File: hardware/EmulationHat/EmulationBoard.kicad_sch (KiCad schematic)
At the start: 4 parts, among them J1 Conn_02x16_Top_Bottom, J2 Conn_02x16_Top_Bottom, Q1 FDN340P, U1 ATmega32U4-M

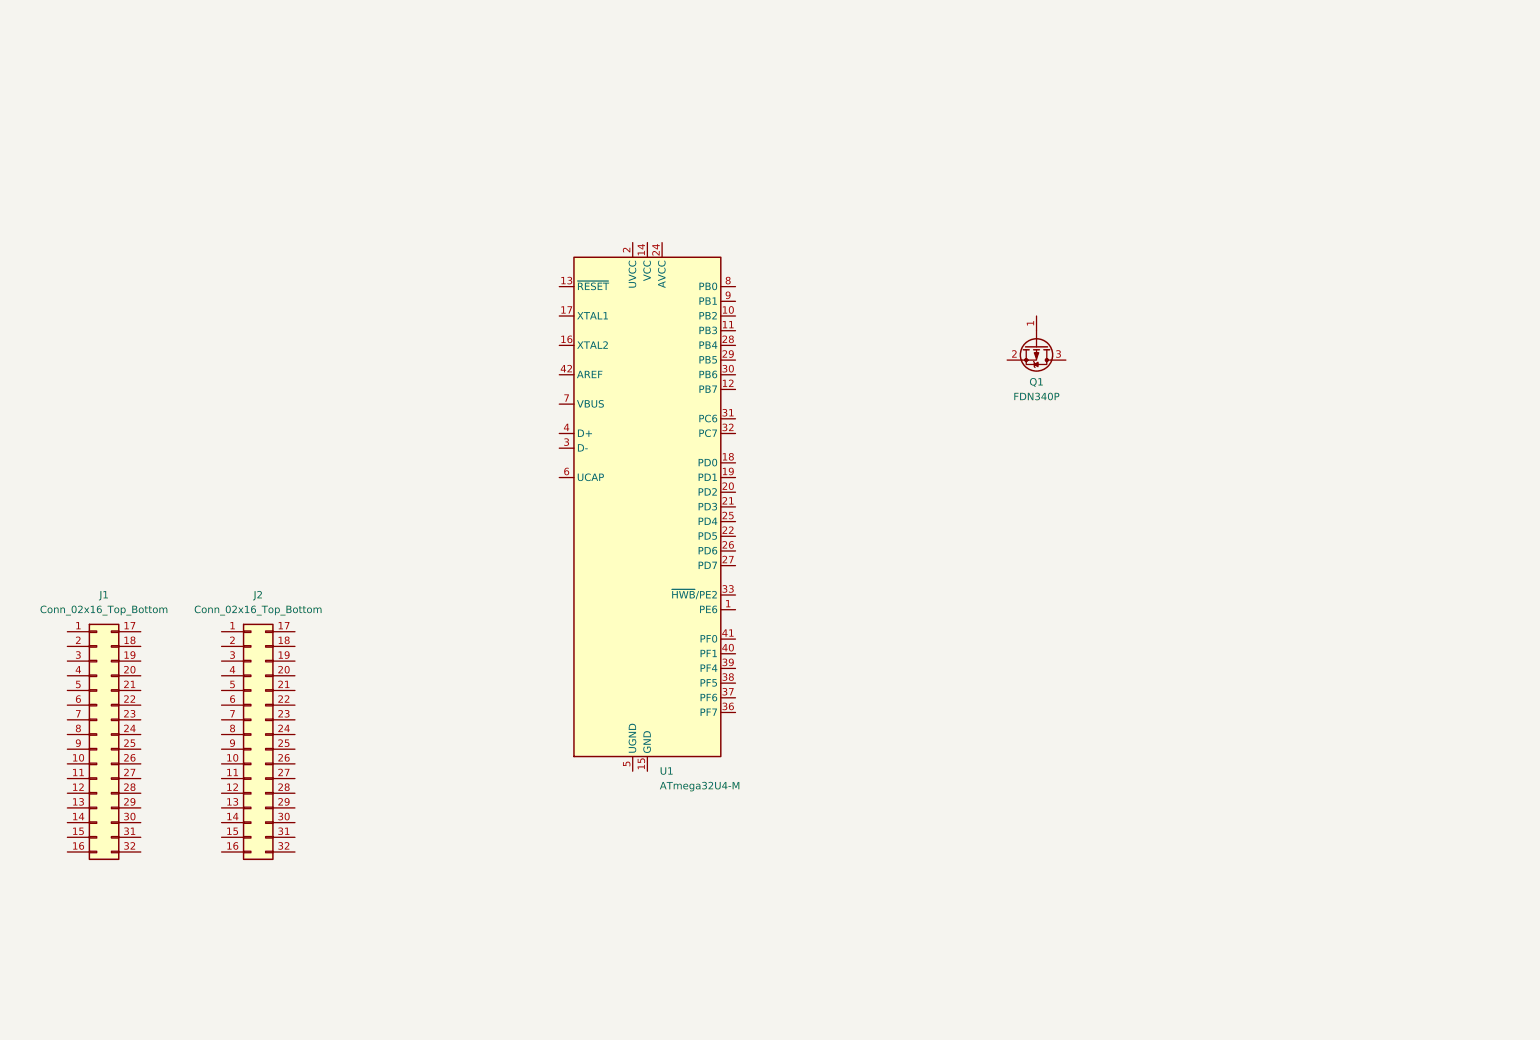
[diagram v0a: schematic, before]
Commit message: started adding subsystems for the emulation hat
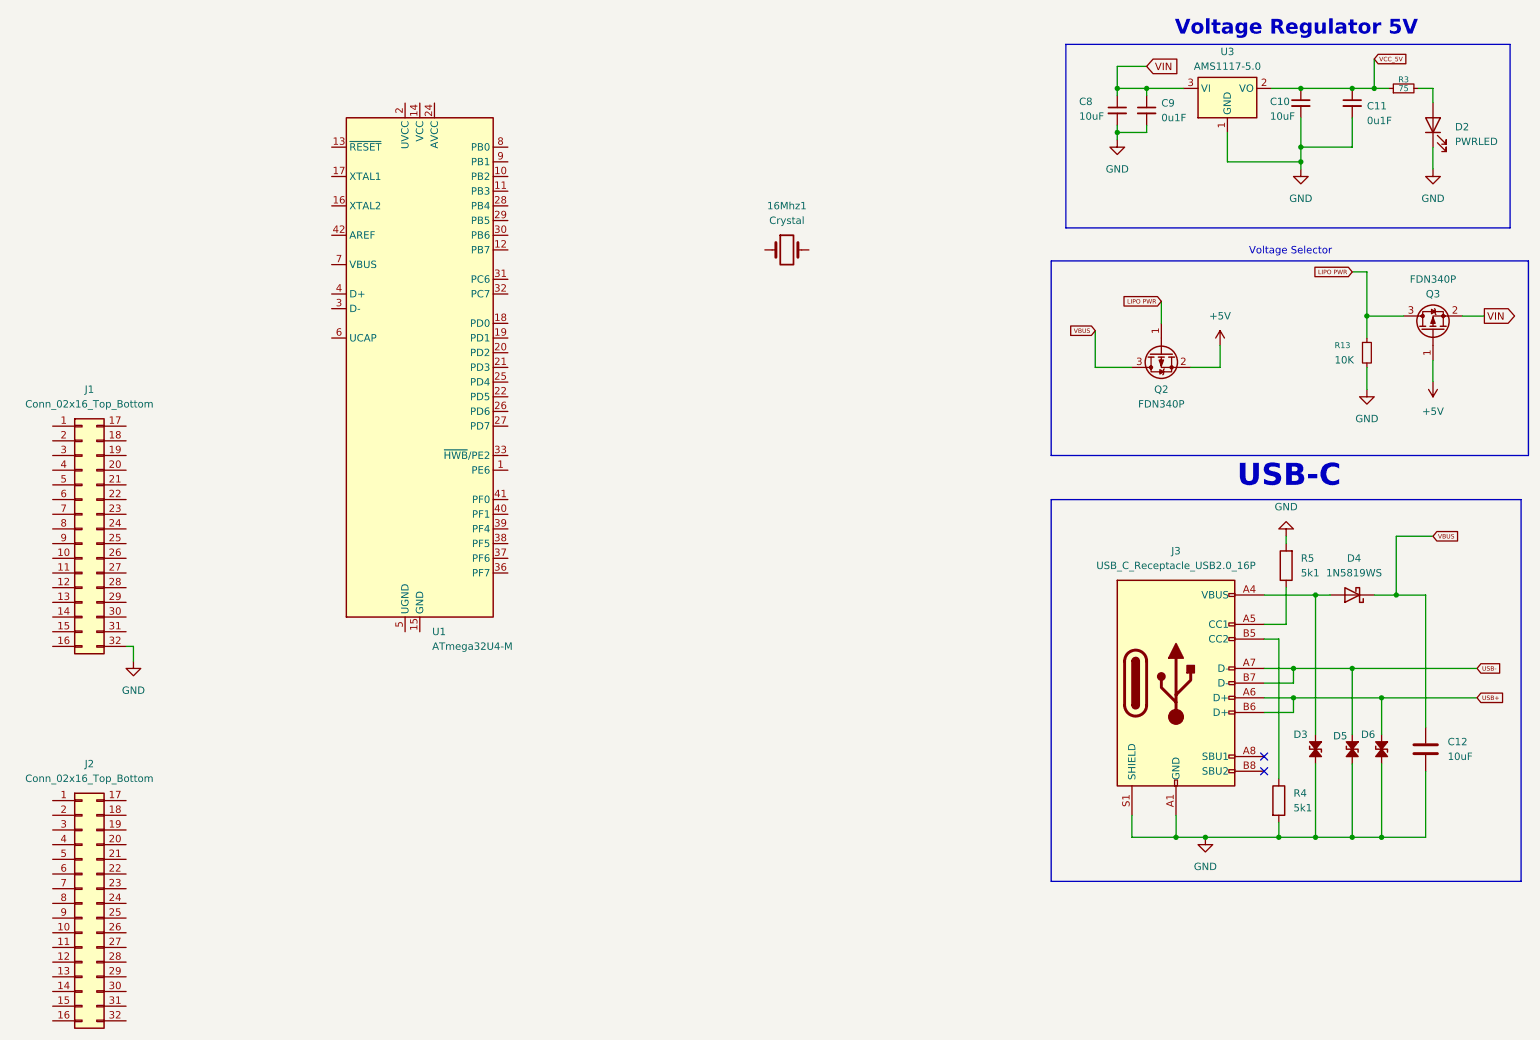
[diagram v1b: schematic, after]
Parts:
- removed Q1: FDN340P, Package_TO_SOT_SMD:SOT-23, symbol Transistor_FET:FDN340P
- added 16Mhz1: Crystal, Crystal:Crystal_SMD_HC49-SD, symbol Device:Crystal
- added C10, C8: 10uF, Capacitor_SMD:C_0603_1608Metric, symbol Device:C_Small
- added C11, C9: 0u1F, Capacitor_SMD:C_0402_1005Metric, symbol Device:C_Small
- added C12: 10uF, Capacitor_SMD:C_0603_1608Metric, symbol Device:C
- added D2: PWRLED, LED_SMD:LED_0603_1608Metric, symbol Device:LED
- added D3, D5, D6: D_TVS_Small_Filled, Diode_SMD:D_0603_1608Metric, symbol Device:D_TVS_Small_Filled
- added D4: 1N5819WS, Diode_SMD:D_SOD-323, symbol Diode:1N5819WS
- added J3: USB_C_Receptacle_USB2.0_16P, Connector_USB:USB_C_Receptacle_GCT_USB4085, symbol Connector:USB_C_Receptacle_USB2.0_16P
- added Q2, Q3: FDN340P, Package_TO_SOT_SMD:SOT-23, symbol Transistor_FET:FDN340P
- added R13: 10K, Resistor_SMD:R_0603_1608Metric, symbol Device:R_Small
- added R3: 75, Resistor_SMD:R_0603_1608Metric, symbol Device:R_Small
- added R4, R5: 5k1, Resistor_SMD:R_0402_1005Metric, symbol Device:R
- added U3: AMS1117-5.0, Package_TO_SOT_SMD:SOT-223-3_TabPin2, symbol Regulator_Linear:AMS1117-5.0
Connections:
- net GND: now reaches J1.32 (Pin_32)
- net GND: now also C10.2, C11.2, C12.2, C8.2, C9.2, D2.1 (K), D3.2 (A2), D5.2 (A2), D6.2 (A2), J3.A1 (GND), J3.A12 (GND), J3.B1 (GND), J3.B12 (GND), J3.S1 (SHIELD), R13.2, R4.2, R5.2, U3.1 (GND)
- new net: J3.A5 (CC1), R5.1
- new net: D3.1 (A1), D4.2 (A), J3.A4 (VBUS), J3.A9 (VBUS), J3.B4 (VBUS), J3.B9 (VBUS)
- new net: J3.B5 (CC2), R4.1
- new net: D2.2 (A), R3.2
- new net +5V: Q2.2 (S), Q3.1 (G)
- new net LIPO PWR: Q2.1 (G), Q3.3 (D), R13.1
- new net USB+: D6.1 (A1), J3.A6 (D+), J3.B6 (D+)
- new net USB-: D5.1 (A1), J3.A7 (D-), J3.B7 (D-)
- new net VBUS: C12.1, D4.1 (K), Q2.3 (D)
- new net VCC_5V: C10.1, C11.1, R3.1, U3.2 (VO)
- new net VIN: C8.1, C9.1, Q3.2 (S), U3.3 (VI)
- no-connect marks 0 -> 2
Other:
- note added: "USB-C"
- note added: "Voltage Regulator 5V"
- note added: "Voltage Selector"
- moved on the sheet: J1, J2, U1

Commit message: more emulation hat stuff
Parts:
- removed 16Mhz1: Crystal, Crystal:Crystal_SMD_HC49-SD, symbol Device:Crystal
- removed C10, C8: 10uF, Capacitor_SMD:C_0603_1608Metric, symbol Device:C_Small
- removed C11, C9: 0u1F, Capacitor_SMD:C_0402_1005Metric, symbol Device:C_Small
- removed D2: PWRLED, LED_SMD:LED_0603_1608Metric, symbol Device:LED
- removed J1: Conn_02x16_Top_Bottom, MolexFSB:FSB5 Series 0.40 mm Pitch Floating SlimStack Board-to-Board Receptacles, symbol Connector_Generic:Conn_02x16_Top_Bottom
- removed J2: Conn_02x16_Top_Bottom, MolexFSB:FSB5 Series 0.40 mm Pitch Floating SlimStack Board-to-Board Plugs, symbol Connector_Generic:Conn_02x16_Top_Bottom
- removed Q2, Q3: FDN340P, Package_TO_SOT_SMD:SOT-23, symbol Transistor_FET:FDN340P
- removed R13: 10K, Resistor_SMD:R_0603_1608Metric, symbol Device:R_Small
- removed R3: 75, Resistor_SMD:R_0603_1608Metric, symbol Device:R_Small
- removed U1: ATmega32U4-M, Package_DFN_QFN:QFN-44-1EP_7x7mm_P0.5mm_EP5.15x5.15mm, symbol MCU_Microchip_ATmega:ATmega32U4-M
- removed U3: AMS1117-5.0, Package_TO_SOT_SMD:SOT-223-3_TabPin2, symbol Regulator_Linear:AMS1117-5.0
- added C1, C2: 22pF, Capacitor_SMD:C_0402_1005Metric, symbol Micro_Rev1j-eagle-import:C-EUC0402
- added C10: 22u, Micro_Rev1j:SMC_B, symbol Micro_Rev1j-eagle-import:CPOL-EUSMCB
- added C12, C3, C5: 1uF, Capacitor_SMD:C_0402_1005Metric, symbol Micro_Rev1j-eagle-import:C-EUC0402
- added C13, C4, C6, C7, C8: 100n, Capacitor_SMD:C_0402_1005Metric, symbol Micro_Rev1j-eagle-import:C-EUC0402
- added D1: CD1206-S01575, Micro_Rev1j:MINIMELF, symbol Micro_Rev1j-eagle-import:DIODE-MINIMELF
- added J1: HEAD17-NOSS, Micro_Rev1j:HEAD17-NOSS, symbol Micro_Rev1j-eagle-import:HEAD17-NOSS
- added J2: HEAD17-NOSS-1, Micro_Rev1j:HEAD17-NOSS-1, symbol Micro_Rev1j-eagle-import:HEAD17-NOSS-1
- added J3: 3x2M, Micro_Rev1j:2X03, symbol Micro_Rev1j-eagle-import:PINHD-2X3
- added L1: MH2029-300Y, Micro_Rev1j:0805, symbol Micro_Rev1j-eagle-import:WE-CBF_0805
- added L2: green, Micro_Rev1j:CHIPLED_0805, symbol Micro_Rev1j-eagle-import:LEDCHIPLED_0805
- added ON1: blue, Micro_Rev1j:CHIPLED_0805, symbol Micro_Rev1j-eagle-import:LEDCHIPLED_0805
- added R1, R6, R7: 10K, Micro_Rev1j:R0402, symbol Micro_Rev1j-eagle-import:R-EU_R0402
- added R2, R3, R4, R5: 1K, Micro_Rev1j:R0402, symbol Micro_Rev1j-eagle-import:R-EU_R0402
- added RESET1: TS42, Micro_Rev1j:TS42, symbol Micro_Rev1j-eagle-import:TS42
- added RP1: 22R, Micro_Rev1j:CAY16, symbol Micro_Rev1j-eagle-import:4R-NCAY16
- added RX1, TX1: yellow, Micro_Rev1j:CHIPLED_0805, symbol Micro_Rev1j-eagle-import:LEDCHIPLED_0805
- added T1: FDN340P/PMV48XP, Micro_Rev1j:SOT-23, symbol Micro_Rev1j-eagle-import:PMOSSOT23
- added T2: PMV48XP, Micro_Rev1j:SOT-23, symbol Micro_Rev1j-eagle-import:PMOSSOT23
- added U$1, U$2: DNP, Micro_Rev1j:FD-1-1.5, symbol Micro_Rev1j-eagle-import:FIDUCIAL-1.5MM
- added U1: ATMEGA32U4-XUMU, Micro_Rev1j:QFN44ML7X7, symbol Micro_Rev1j-eagle-import:ATMEGA32U4-XUMU
- added U2: NCP1117-5, Micro_Rev1j:SOT223, symbol Micro_Rev1j-eagle-import:LINEAR_MC33269ST
- added U3: LP2985-33DBVR, Micro_Rev1j:SOT23-DBV, symbol Micro_Rev1j-eagle-import:LP2985-XXDBVR
- added Y1: 16MHz KX-7, Micro_Rev1j:CRYSTAL-3.2-2.5, symbol Micro_Rev1j-eagle-import:CRYSTAL-3.2-2.5
- renumbered C12 to C14, D3 to D2, D4 to D3, D5 to D4, D6 to D5, J3 to J5, R5 to R10, R4 to R9
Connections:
- net +5V: now also C10.+, C13.1, C6.1, C7.1, D1.C, J2.6, J3.2, L1.1, R1.1, R5.1, T1.2 (S), T2.3 (G), U1.14 (VCC), U1.2 (UVCC), U1.24 (AVCC), U1.34 (VCC1), U2.2 (OUT@1), U2.4 (OUT), U3.1 (IN), U3.3 (ON/~{OFF})
- net GND: now also C1.1, C10.-, C12.2, C13.2, C2.1, C3.2, C4.2, C5.2, C6.2, C7.2, C8.2, J1.6, J2.4, J3.6, L2.C, ON1.C, R6.2, R7.1, RESET1.3, RESET1.4, RESET1.5 (5-GND), RP1.3 (1), RP1.4 (1), RP1.5 (2), RP1.6 (2), RX1.C, TX1.C, U1.15 (GND), U1.23 (GND1), U1.35 (GND2), U1.43 (GND3), U1.5 (UGND), U1.EXP (PAD), U2.1 (GND/ADJ), U3.2 (GND), Y1.2 (GND@1), Y1.4 (GND@2)
- net USB+: now also U1.4 (D+)
- net USB-: now also U1.3 (D-)
- net VIN: now also J2.3, R7.2, T1.3 (G), T2.1 (D)
- net VBUS renamed VUSB
- net VUSB: now also T1.1 (D), U1.7 (VBUS)
- new net: L2.A, R2.2
- new net: ON1.A, R5.2
- new net: R4.2, TX1.A
- new net: R3.2, RX1.A
- new net +VIN: C8.1, T2.2 (S), U2.3 (IN)
- new net 3V3: C12.1, J2.16, U3.5 (OUT)
- new net A0: J2.14, U1.36 ((ADC7/TDI)PF7)
- new net A1: J2.13, U1.37 ((ADC6/TDO)PF6)
- new net A2: J2.12, U1.38 ((ADC5/TMS)PF5)
- new net A3: J2.11, U1.39 ((ADC4/TCK)PF4)
- new net A4: J2.10, U1.40 ((ADC1)PF1)
- new net A5: J2.9, U1.41 ((ADC0)PF0)
- new net AREF: C4.1, J2.15, U1.42 (AREF)
- new net AVCC: C3.1, L1.2, U1.44 (AVCC1)
- new net D0/RX: J1.4, U1.20 ((RXD1/AIN1/INT2)PD2)
- new net D1/TX: J1.3, U1.21 ((TXD1/INT3)PD3)
- new net D2/SDA: J1.7, U1.19 ((SDA/INT1)PD1)
- new net D3/SCL: J1.8, U1.18 ((OC0B/SCL/INT0)PD0)
- new net D4*: J1.9, U1.25 ((ICP1/ADC8)PD4)
- new net D5*: J1.10, U1.31 ((OC3A/#0C4A)PC6)
- new net D6*: J1.11, U1.27 ((T0/OC4D/ADC10)PD7)
- new net D7: J1.12, U1.1 ((INT6/AIN0)PE6)
- new net HWB: R6.1, U1.33 ((#HWB)PE2)
- new net IO10*: J1.15, U1.30 ((PCINT6/OC1B/OC4B/ADC13)PB6)
- new net IO11*: J1.16, U1.12 ((PCINT7/OC0A/OC1C/#RTS)PB7)
- new net IO12*: J1.17, U1.26 ((T1/#OC4D/ADC9)PD6)
- new net IO13*: J2.17, R2.1, U1.32 ((ICP3/CLK0/OC4A)PC7)
- new net IO8: J1.13, U1.28 ((ADC11/PCINT4)PB4)
- new net IO9*: J1.14, U1.29 ((PCINT5/OC1A/#OC4B/ADC12)PB5)
- new net MISO: J2.2, J3.1, U1.11 ((PD0/MISO/PCINT3)PB3)
- new net MOSI: J1.1, J3.4, U1.10 ((PDI/MOSI/PCINT2)PB2)
- new net RESET: D1.A, J1.5, J2.5, J3.5, R1.2, RESET1.1, RESET1.2, U1.13 (RESET)
- new net RXLED/SS: J1.2, R3.1, U1.8 ((SS/PCINT0)PB0)
- new net SCK: J2.1, J3.3, U1.9 ((SCLK/PCINT1)PB1)
- new net TXLED: R4.1, U1.22 ((XCK1/#CTS)PD5)
- new net UCAP: C5.1, U1.6 (UCAP)
- new net XTAL1: C2.2, U1.17 (XTAL1), Y1.3 (C2)
- new net XTAL2: C1.2, U1.16 (XTAL2), Y1.1 (C1)
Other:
- note added: "#PWM 10bit"
- note added: "#PWM 16bit"
- note added: "#PWM 8/16bit"
- note added: "#PWM 8bit"
- note added: "#PWM Hi-Speed"
- note added: "+3V3 REG"
- note added: "+5V REG"
- note added: "+5V SELECTOR (USB)"
- note added: "ICSP"
- note added: "NOT USED"
- note removed: "Voltage Regulator 5V"
- note removed: "Voltage Selector"

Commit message: emulation
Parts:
- removed C1, C2: 22pF, Capacitor_SMD:C_0402_1005Metric, symbol Micro_Rev1j-eagle-import:C-EUC0402
- removed C10: 22u, Micro_Rev1j:SMC_B, symbol Micro_Rev1j-eagle-import:CPOL-EUSMCB
- removed C12, C3, C5: 1uF, Capacitor_SMD:C_0402_1005Metric, symbol Micro_Rev1j-eagle-import:C-EUC0402
- removed C13, C4, C6, C7, C8: 100n, Capacitor_SMD:C_0402_1005Metric, symbol Micro_Rev1j-eagle-import:C-EUC0402
- removed D1: CD1206-S01575, Micro_Rev1j:MINIMELF, symbol Micro_Rev1j-eagle-import:DIODE-MINIMELF
- removed J1: HEAD17-NOSS, Micro_Rev1j:HEAD17-NOSS, symbol Micro_Rev1j-eagle-import:HEAD17-NOSS
- removed J2: HEAD17-NOSS-1, Micro_Rev1j:HEAD17-NOSS-1, symbol Micro_Rev1j-eagle-import:HEAD17-NOSS-1
- removed J3: 3x2M, Micro_Rev1j:2X03, symbol Micro_Rev1j-eagle-import:PINHD-2X3
- removed L1: MH2029-300Y, Micro_Rev1j:0805, symbol Micro_Rev1j-eagle-import:WE-CBF_0805
- removed L2: green, Micro_Rev1j:CHIPLED_0805, symbol Micro_Rev1j-eagle-import:LEDCHIPLED_0805
- removed ON1: blue, Micro_Rev1j:CHIPLED_0805, symbol Micro_Rev1j-eagle-import:LEDCHIPLED_0805
- removed R1, R6, R7: 10K, Micro_Rev1j:R0402, symbol Micro_Rev1j-eagle-import:R-EU_R0402
- removed R2, R3, R4, R5: 1K, Micro_Rev1j:R0402, symbol Micro_Rev1j-eagle-import:R-EU_R0402
- removed RESET1: TS42, Micro_Rev1j:TS42, symbol Micro_Rev1j-eagle-import:TS42
- removed RP1: 22R, Micro_Rev1j:CAY16, symbol Micro_Rev1j-eagle-import:4R-NCAY16
- removed RX1, TX1: yellow, Micro_Rev1j:CHIPLED_0805, symbol Micro_Rev1j-eagle-import:LEDCHIPLED_0805
- removed T1: FDN340P/PMV48XP, Micro_Rev1j:SOT-23, symbol Micro_Rev1j-eagle-import:PMOSSOT23
- removed T2: PMV48XP, Micro_Rev1j:SOT-23, symbol Micro_Rev1j-eagle-import:PMOSSOT23
- removed U$1, U$2: DNP, Micro_Rev1j:FD-1-1.5, symbol Micro_Rev1j-eagle-import:FIDUCIAL-1.5MM
- removed U1: ATMEGA32U4-XUMU, Micro_Rev1j:QFN44ML7X7, symbol Micro_Rev1j-eagle-import:ATMEGA32U4-XUMU
- removed U2: NCP1117-5, Micro_Rev1j:SOT223, symbol Micro_Rev1j-eagle-import:LINEAR_MC33269ST
- removed U3: LP2985-33DBVR, Micro_Rev1j:SOT23-DBV, symbol Micro_Rev1j-eagle-import:LP2985-XXDBVR
- removed Y1: 16MHz KX-7, Micro_Rev1j:CRYSTAL-3.2-2.5, symbol Micro_Rev1j-eagle-import:CRYSTAL-3.2-2.5
- added C10, C8: 10uF, Capacitor_SMD:C_0603_1608Metric, symbol Device:C_Small
- added C11, C9: 0u1F, Capacitor_SMD:C_0402_1005Metric, symbol Device:C_Small
- added D1: PWRLED, LED_SMD:LED_0603_1608Metric, symbol Device:LED
- added Q2, Q3: FDN340P, Package_TO_SOT_SMD:SOT-23, symbol Transistor_FET:FDN340P
- added R13: 10K, Resistor_SMD:R_0603_1608Metric, symbol Device:R_Small
- added R3: 75, Resistor_SMD:R_0603_1608Metric, symbol Device:R_Small
- added U3: AMS1117-5.0, Package_TO_SOT_SMD:SOT-223-3_TabPin2, symbol Regulator_Linear:AMS1117-5.0
- added Y1: Crystal, Crystal:Crystal_HC49-4H_Vertical, symbol Device:Crystal
- added Y2: Resonator, symbol Device:Resonator
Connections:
- net +5V: now also Q2.2 (S), Q3.1 (G)
- net GND: now also C10.2, C11.2, C8.2, C9.2, D1.1 (K), R13.2, U3.1 (GND)
- net VIN: now also C8.1, C9.1, Q3.2 (S), U3.3 (VI)
- new net: D1.2 (A), R3.2
- new net LIPO PWR: Q2.1 (G), Q3.3 (D), R13.1
- new net VBUS: Q2.3 (D)
- new net VCC_5V: C10.1, C11.1, R3.1, U3.2 (VO)
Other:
- note added: "Voltage Regulator 5V"
- note added: "Voltage Selector"
- note removed: "#PWM 10bit"
- note removed: "#PWM 16bit"
- note removed: "#PWM 8/16bit"
- note removed: "#PWM 8bit"
- note removed: "#PWM Hi-Speed"
- note removed: "+3V3 REG"
- note removed: "+5V REG"
- note removed: "+5V SELECTOR (USB)"
- note removed: "ICSP"
- note removed: "NOT USED"

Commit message: correct connector placement
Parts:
- removed Y1: Crystal, Crystal:Crystal_HC49-4H_Vertical, symbol Device:Crystal
- added C1, C2: 100nF, Capacitor_SMD:C_0603_1608Metric, symbol Device:C_Small
- added D6: TXLED, LED_SMD:LED_0603_1608Metric, symbol Device:LED
- added D7: RXLED, LED_SMD:LED_0603_1608Metric, symbol Device:LED
- added D8: LED, LED_SMD:LED_0603_1608Metric, symbol Device:LED
- added J1: Conn_02x16_Top_Bottom, MolexFSB:FSB5 Series 0.40 mm Pitch Floating SlimStack Board-to-Board Receptacles, symbol Connector_Generic:Conn_02x16_Top_Bottom
- added J2: Conn_02x16_Top_Bottom, MolexFSB:FSB5 Series 0.40 mm Pitch Floating SlimStack Board-to-Board Plugs, symbol Connector_Generic:Conn_02x16_Top_Bottom
- added R1, R2, R4, R5, R6, R7: 1k, Resistor_SMD:R_0603_1608Metric, symbol Device:R_Small
- added SW1: SW_Push, Button_Switch_SMD:SW_SPST_CK_RS282G05A3, symbol Switch:SW_Push
- added U1: ATmega328P-M, Package_DFN_QFN:QFN-32-1EP_5x5mm_P0.5mm_EP3.1x3.1mm, symbol MCU_Microchip_ATmega:ATmega328P-M
- added U2: FT232RL, Package_SO:SSOP-28_5.3x10.2mm_P0.65mm, symbol Interface_USB:FT232RL
- Y2: footprint (none) -> Crystal:Resonator_SMD_Murata_CSTxExxV-3Pin_3.0x1.1mm
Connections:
- net VCC_5V is gone; now on net +5V: C10.1, C11.1, R3.1, U3.2 (VO)
- net VUSB is gone; now on net VBUS: C14.1, D3.1 (K)
- net +5V: now also D6.2 (A), D7.2 (A), R7.1, U1.18 (AVCC), U1.4 (VCC), U1.6 (VCC), U2.20 (VCC), U2.4 (VCCIO)
- net GND: now also Y2.2, C1.2, D8.1 (K), J1.32 (Pin_32), J2.32 (Pin_32), SW1.1, U1.21 (GND), U1.3 (GND), U1.33 (GND), U1.5 (GND), U2.18 (GND), U2.21 (GND), U2.25 (AGND), U2.26 (TEST), U2.7 (GND)
- net USB+: now also U2.15 (USBD+)
- net USB-: now also U2.16 (USBD-)
- net VIN: now also J1.31 (Pin_31), J2.31 (Pin_31)
- net at Y2.1: now also U1.7 (XTAL1/PB6)
- net at Y2.3: now also U1.8 (XTAL2/PB7)
- new net: R1.1, U2.22 (CBUS1)
- new net: D6.1 (K), R1.2
- new net: C2.1, U2.2 (DTR)
- new net: R6.2, U1.17 (PB5)
- new net: C1.1, U1.20 (AREF)
- new net: R4.1, U1.30 (PD0)
- new net: R5.1, U1.31 (PD1)
- new net: D8.2 (A), R6.1
- new net: D7.1 (K), R2.2
- new net: R2.1, U2.23 (CBUS0)
- new net CONN_0: J1.1 (Pin_1), J2.16 (Pin_16)
- new net CONN_1: J1.2 (Pin_2), J2.17 (Pin_17)
- new net CONN_10: J1.11 (Pin_11), J2.26 (Pin_26)
- new net CONN_11: J1.12 (Pin_12), J2.27 (Pin_27)
- new net CONN_12: J1.13 (Pin_13), J2.28 (Pin_28)
- new net CONN_13: J1.14 (Pin_14), J2.29 (Pin_29)
- new net CONN_14: J1.15 (Pin_15), J2.30 (Pin_30)
- new net CONN_15: J1.16 (Pin_16), J2.1 (Pin_1)
- new net CONN_16: J1.17 (Pin_17), J2.2 (Pin_2)
- new net CONN_17: J1.18 (Pin_18), J2.3 (Pin_3)
- new net CONN_18: J1.19 (Pin_19), J2.4 (Pin_4)
- new net CONN_19: J1.20 (Pin_20), J2.5 (Pin_5)
- new net CONN_2: J1.3 (Pin_3), J2.18 (Pin_18)
- new net CONN_20: J1.21 (Pin_21), J2.6 (Pin_6)
- new net CONN_21: J1.22 (Pin_22), J2.7 (Pin_7)
- new net CONN_22: J1.23 (Pin_23), J2.8 (Pin_8)
- new net CONN_23: J1.24 (Pin_24), J2.9 (Pin_9)
- new net CONN_24: J1.25 (Pin_25), J2.10 (Pin_10)
- new net CONN_25: J1.26 (Pin_26), J2.11 (Pin_11)
- new net CONN_26: J1.27 (Pin_27), J2.12 (Pin_12)
- new net CONN_27: J1.28 (Pin_28), J2.13 (Pin_13)
- new net CONN_28: J1.29 (Pin_29), J2.14 (Pin_14)
- new net CONN_29: J1.30 (Pin_30), J2.15 (Pin_15)
- new net CONN_3: J1.4 (Pin_4), J2.19 (Pin_19)
- new net CONN_4: J1.5 (Pin_5), J2.20 (Pin_20)
- new net CONN_5: J1.6 (Pin_6), J2.21 (Pin_21)
- new net CONN_6: J1.7 (Pin_7), J2.22 (Pin_22)
- new net CONN_7: J1.8 (Pin_8), J2.23 (Pin_23)
- new net CONN_8: J1.9 (Pin_9), J2.24 (Pin_24)
- new net CONN_9: J1.10 (Pin_10), J2.25 (Pin_25)
- new net RESET: C2.2, R7.2, SW1.2, U1.29 (~{RESET}/PC6)
- new net RX: R4.2, U2.1 (TXD)
- new net TX: R5.2, U2.5 (RXD)
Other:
- moved on the sheet: Y2
